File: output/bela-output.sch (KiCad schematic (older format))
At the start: 55 parts, among them P1 in_bela, P2 MTA-156-4, P3 out_mod, U1 TL074, U2 TL074, U3 TL072

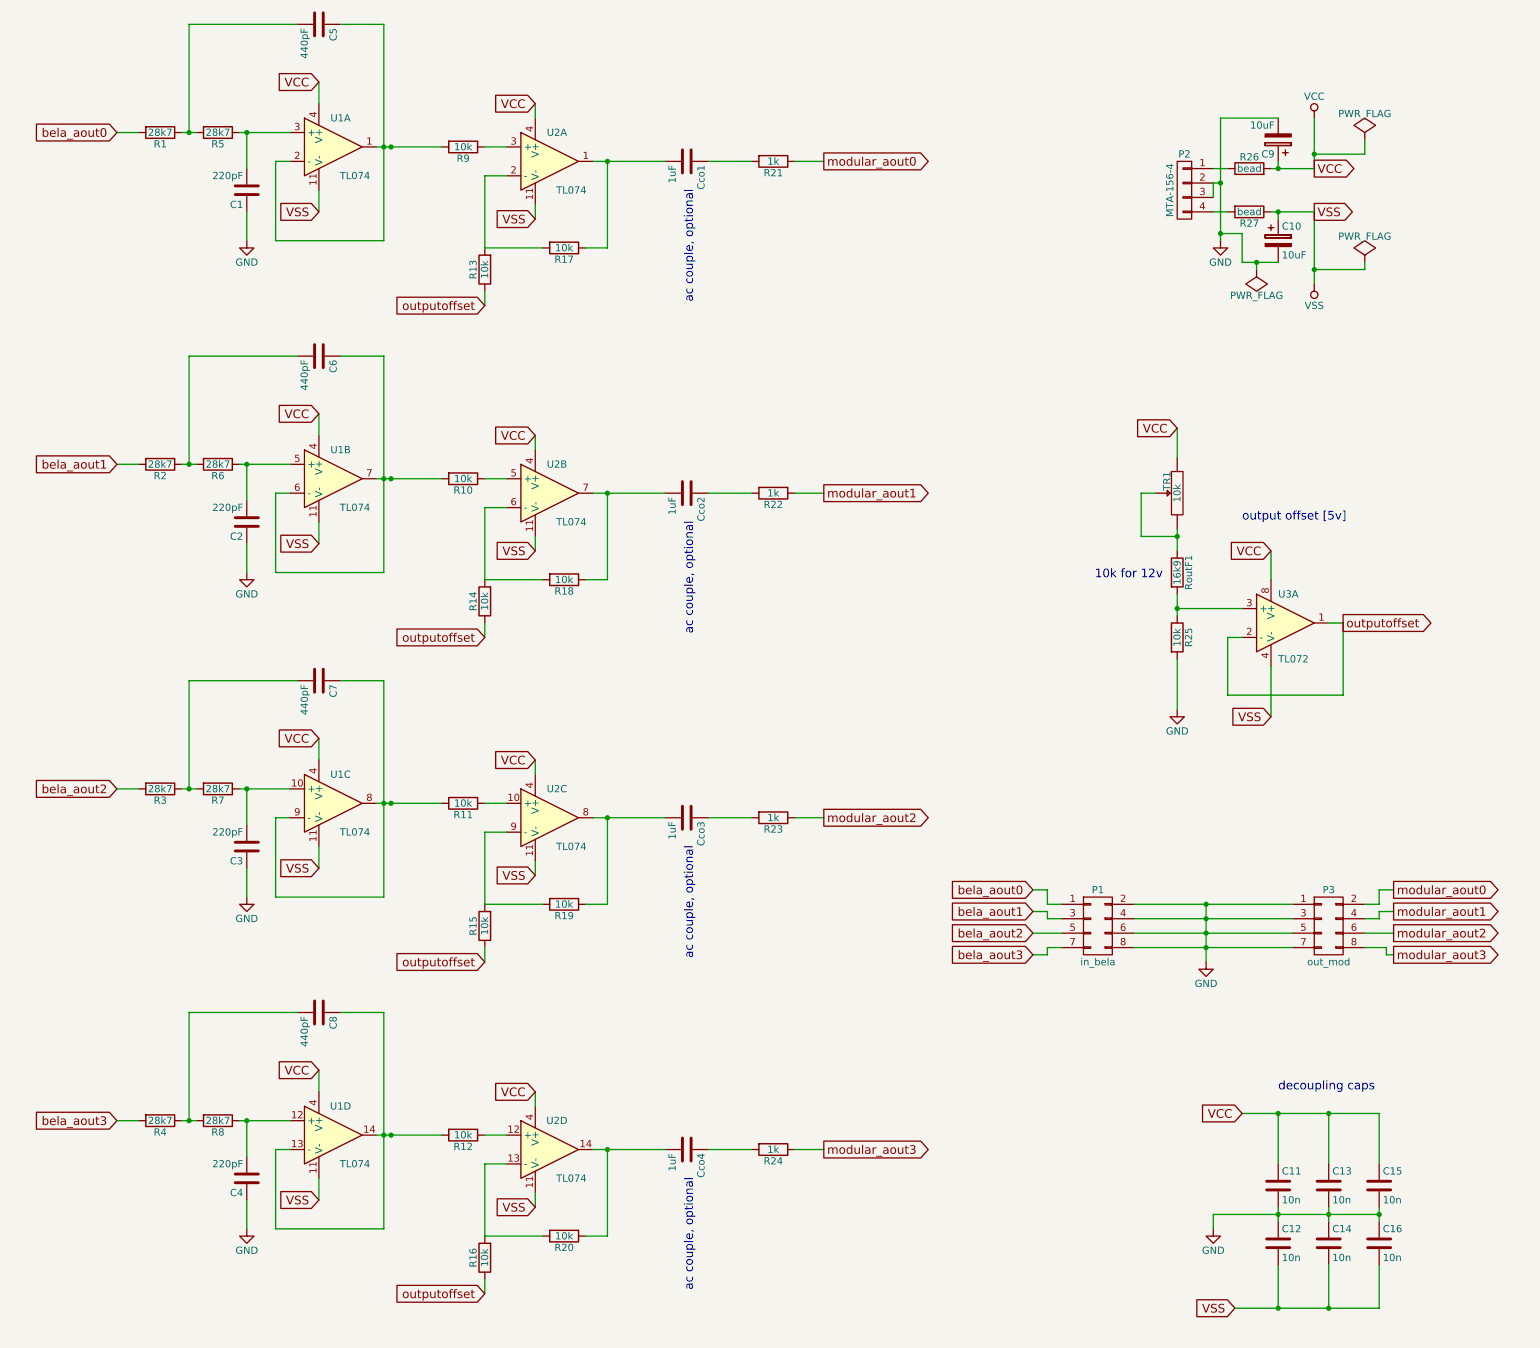
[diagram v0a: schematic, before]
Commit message: flush resistor layout
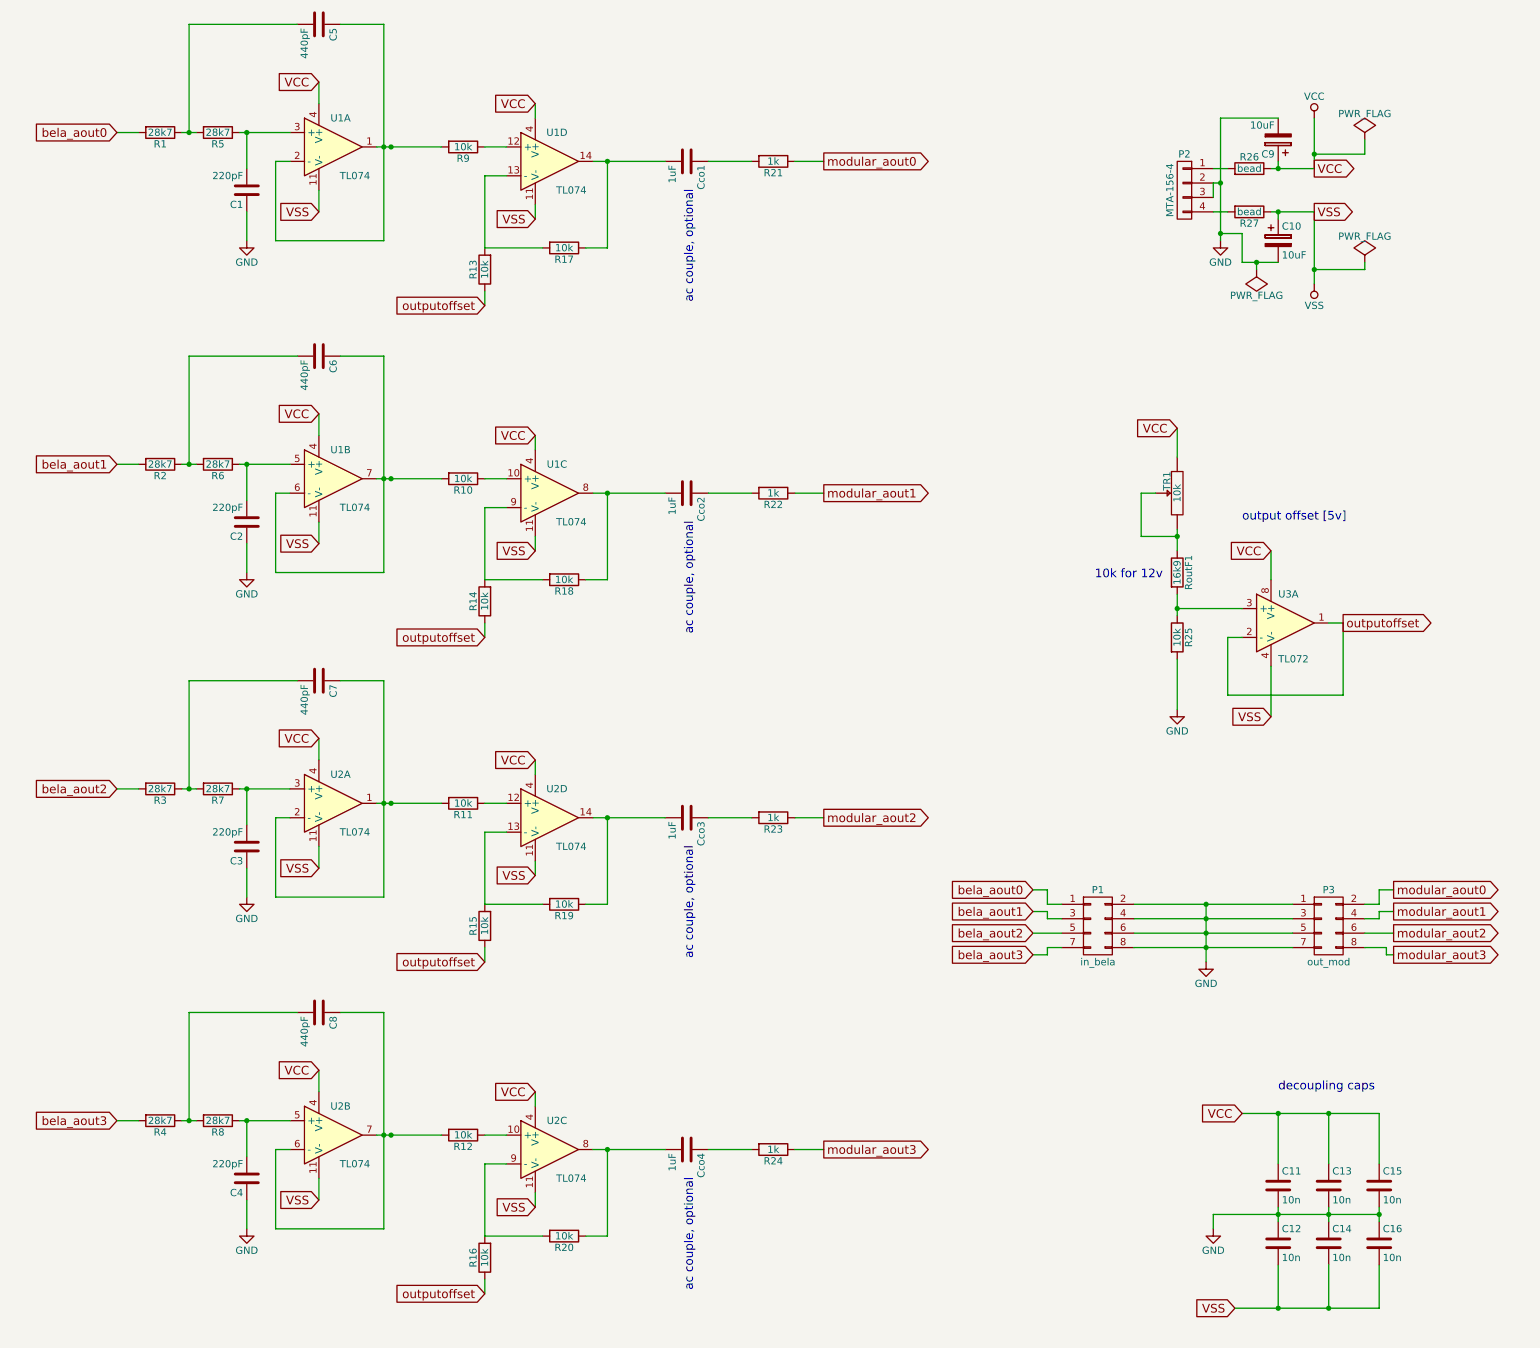
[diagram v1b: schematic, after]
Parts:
- R1, R10, R11, R12, R13, R14, R15, R16, R17, R18, R19, R2, R20, R21, R22, R23, R24, R25, R3, R4, R5, R6, R7, R8, R9, RoutF1: footprint Resistors_ThroughHole:Resistor_Vertical_RM5mm -> Resistors_ThroughHole:Resistor_Horizontal_RM10mm
- renumbered U2 to U1, U1 to U2
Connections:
- net VCC: now also R26.1; no longer R26.2
- net at Cco1.2, R17.1: now also U1.14; no longer U1.1
- net at R9.1: now also U1.12 (+); no longer U1.3 (+)
- net at R13.2, R17.2: now also U1.13 (-); no longer U1.2 (-)
- net at Cco2.2, R18.1: now also U1.8; no longer U1.7
- net at R10.1: now also U1.10 (+); no longer U1.5 (+)
- net at R14.2, R18.2: now also U1.9 (-); no longer U1.6 (-)
- net at Cco3.2, R19.1: now also U2.14; no longer U2.8
- net at R11.1: now also U2.12 (+); no longer U2.10 (+)
- net at C7.1, R11.2: now also U2.1, U2.2 (-); no longer U2.8, U2.9 (-)
- net at R15.2, R19.2: now also U2.13 (-); no longer U2.9 (-)
- net at C3.2, R7.1: now also U2.3 (+); no longer U2.10 (+)
- net at Cco4.2, R20.1: now also U2.8; no longer U2.14
- net at R12.1: now also U2.10 (+); no longer U2.12 (+)
- net at C8.1, R12.2: now also U2.6 (-), U2.7; no longer U2.13 (-), U2.14
- net at R16.2, R20.2: now also U2.9 (-); no longer U2.13 (-)
- net at C4.2, R8.1: now also U2.5 (+); no longer U2.12 (+)
- net at P2.1 (P1): now also R26.2; no longer R26.1
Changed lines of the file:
@@
 LIBS:trim
 LIBS:bela-output-cache
-LIBS:bela-input-cache
 EELAYER 25 0
 EELAYER END
@@
 F 0 "R9" V 3580 1600 50  0000 C CNN
 F 1 "10k" V 3500 1600 50  0000 C CNN
-F 2 "Resistors_ThroughHole:Resistor_Vertical_RM5mm" V 3430 1600 50  0001 C CNN
+F 2 "Resistors_ThroughHole:Resistor_Horizontal_RM10mm" V 3430 1600 50  0001 C CNN
 F 3 "" H 3500 1600 50  0000 C CNN
 	1    3500 1600
@@
 F 0 "R13" V 3730 2450 50  0000 C CNN
 F 1 "10k" V 3650 2450 50  0000 C CNN
-F 2 "Resistors_ThroughHole:Resistor_Vertical_RM5mm" V 3580 2450 50  0001 C CNN
+F 2 "Resistors_ThroughHole:Resistor_Horizontal_RM10mm" V 3580 2450 50  0001 C CNN
 F 3 "" H 3650 2450 50  0000 C CNN
 	1    3650 2450
@@
 $EndComp
 $Comp
-L TL074 U2
-U 1 1 5846D2B4
+L TL074 U1
+U 4 1 5846D2B4
 P 4100 1700
-F 0 "U2" H 4150 1900 50  0000 C CNN
+F 0 "U1" H 4150 1900 50  0000 C CNN
 F 1 "TL074" H 4250 1500 50  0000 C CNN
 F 2 "Housings_DIP:DIP-14_W7.62mm_LongPads" H 4050 1800 50  0001 C CNN
 F 3 "" H 4150 1900 50  0000 C CNN
-	1    4100 1700
+	4    4100 1700
 	1    0    0    -1
 $EndComp
@@
 F 0 "R17" V 4280 2300 50  0000 C CNN
 F 1 "10k" V 4200 2300 50  0000 C CNN
-F 2 "Resistors_ThroughHole:Resistor_Vertical_RM5mm" V 4130 2300 50  0001 C CNN
+F 2 "Resistors_ThroughHole:Resistor_Horizontal_RM10mm" V 4130 2300 50  0001 C CNN
 F 3 "" H 4200 2300 50  0000 C CNN
 	1    4200 2300
@@
 F 0 "R1" V 1480 1500 50  0000 C CNN
 F 1 "28k7" V 1400 1500 50  0000 C CNN
-F 2 "Resistors_ThroughHole:Resistor_Vertical_RM5mm" V 1330 1500 50  0001 C CNN
+F 2 "Resistors_ThroughHole:Resistor_Horizontal_RM10mm" V 1330 1500 50  0001 C CNN
 F 3 "" H 1400 1500 50  0000 C CNN
 	1    1400 1500
@@
 F 0 "R5" V 1880 1500 50  0000 C CNN
 F 1 "28k7" V 1800 1500 50  0000 C CNN
-F 2 "Resistors_ThroughHole:Resistor_Vertical_RM5mm" V 1730 1500 50  0001 C CNN
+F 2 "Resistors_ThroughHole:Resistor_Horizontal_RM10mm" V 1730 1500 50  0001 C CNN
 F 3 "" H 1800 1500 50  0000 C CNN
 	1    1800 1500
@@
 F 0 "R21" V 5730 1700 50  0000 C CNN
 F 1 "1k" V 5650 1700 50  0000 C CNN
-F 2 "Resistors_ThroughHole:Resistor_Vertical_RM5mm" V 5580 1700 50  0001 C CNN
+F 2 "Resistors_ThroughHole:Resistor_Horizontal_RM10mm" V 5580 1700 50  0001 C CNN
 F 3 "" H 5650 1700 50  0000 C CNN
 	1    5650 1700
@@
 F 0 "R10" V 3580 3900 50  0000 C CNN
 F 1 "10k" V 3500 3900 50  0000 C CNN
-F 2 "Resistors_ThroughHole:Resistor_Vertical_RM5mm" V 3430 3900 50  0001 C CNN
+F 2 "Resistors_ThroughHole:Resistor_Horizontal_RM10mm" V 3430 3900 50  0001 C CNN
 F 3 "" H 3500 3900 50  0000 C CNN
 	1    3500 3900
@@
 F 0 "R14" V 3730 4750 50  0000 C CNN
 F 1 "10k" V 3650 4750 50  0000 C CNN
-F 2 "Resistors_ThroughHole:Resistor_Vertical_RM5mm" V 3580 4750 50  0001 C CNN
+F 2 "Resistors_ThroughHole:Resistor_Horizontal_RM10mm" V 3580 4750 50  0001 C CNN
 F 3 "" H 3650 4750 50  0000 C CNN
 	1    3650 4750
@@
 $EndComp
 $Comp
-L TL074 U2
-U 2 1 5846D2C0
+L TL074 U1
+U 3 1 5846D2C0
 P 4100 4000
-F 0 "U2" H 4150 4200 50  0000 C CNN
+F 0 "U1" H 4150 4200 50  0000 C CNN
 F 1 "TL074" H 4250 3800 50  0000 C CNN
 F 2 "Housings_DIP:DIP-14_W7.62mm_LongPads" H 4050 4100 50  0001 C CNN
 F 3 "" H 4150 4200 50  0000 C CNN
-	2    4100 4000
+	3    4100 4000
 	1    0    0    -1
 $EndComp
@@
 F 0 "R18" V 4280 4600 50  0000 C CNN
 F 1 "10k" V 4200 4600 50  0000 C CNN
-F 2 "Resistors_ThroughHole:Resistor_Vertical_RM5mm" V 4130 4600 50  0001 C CNN
+F 2 "Resistors_ThroughHole:Resistor_Horizontal_RM10mm" V 4130 4600 50  0001 C CNN
 F 3 "" H 4200 4600 50  0000 C CNN
 	1    4200 4600
@@
 F 0 "R2" V 1480 3800 50  0000 C CNN
 F 1 "28k7" V 1400 3800 50  0000 C CNN
-F 2 "Resistors_ThroughHole:Resistor_Vertical_RM5mm" V 1330 3800 50  0001 C CNN
+F 2 "Resistors_ThroughHole:Resistor_Horizontal_RM10mm" V 1330 3800 50  0001 C CNN
 F 3 "" H 1400 3800 50  0000 C CNN
 	1    1400 3800
@@
 F 0 "R6" V 1880 3800 50  0000 C CNN
 F 1 "28k7" V 1800 3800 50  0000 C CNN
-F 2 "Resistors_ThroughHole:Resistor_Vertical_RM5mm" V 1730 3800 50  0001 C CNN
+F 2 "Resistors_ThroughHole:Resistor_Horizontal_RM10mm" V 1730 3800 50  0001 C CNN
 F 3 "" H 1800 3800 50  0000 C CNN
 	1    1800 3800
@@
 F 0 "R22" V 5730 4000 50  0000 C CNN
 F 1 "1k" V 5650 4000 50  0000 C CNN
-F 2 "Resistors_ThroughHole:Resistor_Vertical_RM5mm" V 5580 4000 50  0001 C CNN
+F 2 "Resistors_ThroughHole:Resistor_Horizontal_RM10mm" V 5580 4000 50  0001 C CNN
 F 3 "" H 5650 4000 50  0000 C CNN
 	1    5650 4000
@@
 F 0 "R11" V 3580 6150 50  0000 C CNN
 F 1 "10k" V 3500 6150 50  0000 C CNN
-F 2 "Resistors_ThroughHole:Resistor_Vertical_RM5mm" V 3430 6150 50  0001 C CNN
+F 2 "Resistors_ThroughHole:Resistor_Horizontal_RM10mm" V 3430 6150 50  0001 C CNN
 F 3 "" H 3500 6150 50  0000 C CNN
 	1    3500 6150
@@
 F 0 "R15" V 3730 7000 50  0000 C CNN
 F 1 "10k" V 3650 7000 50  0000 C CNN
-F 2 "Resistors_ThroughHole:Resistor_Vertical_RM5mm" V 3580 7000 50  0001 C CNN
+F 2 "Resistors_ThroughHole:Resistor_Horizontal_RM10mm" V 3580 7000 50  0001 C CNN
 F 3 "" H 3650 7000 50  0000 C CNN
 	1    3650 7000
@@
 $Comp
 L TL074 U2
-U 3 1 5846D2CC
+U 4 1 5846D2CC
 P 4100 6250
 F 0 "U2" H 4150 6450 50  0000 C CNN
@@
 F 2 "Housings_DIP:DIP-14_W7.62mm_LongPads" H 4050 6350 50  0001 C CNN
 F 3 "" H 4150 6450 50  0000 C CNN
-	3    4100 6250
-	1    0    0    -1
-$EndComp
-$Comp
-L TL074 U1
-U 3 1 5846D2CD
+	4    4100 6250
+	1    0    0    -1
+$EndComp
+$Comp
+L TL074 U2
+U 1 1 5846D2CD
 P 2600 6150
-F 0 "U1" H 2650 6350 50  0000 C CNN
+F 0 "U2" H 2650 6350 50  0000 C CNN
 F 1 "TL074" H 2750 5950 50  0000 C CNN
 F 2 "Housings_DIP:DIP-14_W7.62mm_LongPads" H 2550 6250 50  0001 C CNN
 F 3 "" H 2650 6350 50  0000 C CNN
-	3    2600 6150
+	1    2600 6150
 	1    0    0    -1
 $EndComp
@@
 F 0 "R19" V 4280 6850 50  0000 C CNN
 F 1 "10k" V 4200 6850 50  0000 C CNN
-F 2 "Resistors_ThroughHole:Resistor_Vertical_RM5mm" V 4130 6850 50  0001 C CNN
+F 2 "Resistors_ThroughHole:Resistor_Horizontal_RM10mm" V 4130 6850 50  0001 C CNN
 F 3 "" H 4200 6850 50  0000 C CNN
 	1    4200 6850
@@
 F 0 "R3" V 1480 6050 50  0000 C CNN
 F 1 "28k7" V 1400 6050 50  0000 C CNN
-F 2 "Resistors_ThroughHole:Resistor_Vertical_RM5mm" V 1330 6050 50  0001 C CNN
+F 2 "Resistors_ThroughHole:Resistor_Horizontal_RM10mm" V 1330 6050 50  0001 C CNN
 F 3 "" H 1400 6050 50  0000 C CNN
 	1    1400 6050
@@
 F 0 "R7" V 1880 6050 50  0000 C CNN
 F 1 "28k7" V 1800 6050 50  0000 C CNN
-F 2 "Resistors_ThroughHole:Resistor_Vertical_RM5mm" V 1730 6050 50  0001 C CNN
+F 2 "Resistors_ThroughHole:Resistor_Horizontal_RM10mm" V 1730 6050 50  0001 C CNN
 F 3 "" H 1800 6050 50  0000 C CNN
 	1    1800 6050
@@
 F 0 "R23" V 5730 6250 50  0000 C CNN
 F 1 "1k" V 5650 6250 50  0000 C CNN
-F 2 "Resistors_ThroughHole:Resistor_Vertical_RM5mm" V 5580 6250 50  0001 C CNN
+F 2 "Resistors_ThroughHole:Resistor_Horizontal_RM10mm" V 5580 6250 50  0001 C CNN
 F 3 "" H 5650 6250 50  0000 C CNN
 	1    5650 6250
@@
 F 0 "R12" V 3580 8450 50  0000 C CNN
 F 1 "10k" V 3500 8450 50  0000 C CNN
-F 2 "Resistors_ThroughHole:Resistor_Vertical_RM5mm" V 3430 8450 50  0001 C CNN
+F 2 "Resistors_ThroughHole:Resistor_Horizontal_RM10mm" V 3430 8450 50  0001 C CNN
 F 3 "" H 3500 8450 50  0000 C CNN
 	1    3500 8450
@@
 F 0 "R16" V 3730 9300 50  0000 C CNN
 F 1 "10k" V 3650 9300 50  0000 C CNN
-F 2 "Resistors_ThroughHole:Resistor_Vertical_RM5mm" V 3580 9300 50  0001 C CNN
+F 2 "Resistors_ThroughHole:Resistor_Horizontal_RM10mm" V 3580 9300 50  0001 C CNN
 F 3 "" H 3650 9300 50  0000 C CNN
 	1    3650 9300
@@
 $Comp
 L TL074 U2
-U 4 1 5846D2D8
+U 3 1 5846D2D8
 P 4100 8550
 F 0 "U2" H 4150 8750 50  0000 C CNN
@@
 F 2 "Housings_DIP:DIP-14_W7.62mm_LongPads" H 4050 8650 50  0001 C CNN
 F 3 "" H 4150 8750 50  0000 C CNN
-	4    4100 8550
-	1    0    0    -1
-$EndComp
-$Comp
-L TL074 U1
-U 4 1 5846D2D9
+	3    4100 8550
+	1    0    0    -1
+$EndComp
+$Comp
+L TL074 U2
+U 2 1 5846D2D9
 P 2600 8450
-F 0 "U1" H 2650 8650 50  0000 C CNN
+F 0 "U2" H 2650 8650 50  0000 C CNN
 F 1 "TL074" H 2750 8250 50  0000 C CNN
 F 2 "Housings_DIP:DIP-14_W7.62mm_LongPads" H 2550 8550 50  0001 C CNN
 F 3 "" H 2650 8650 50  0000 C CNN
-	4    2600 8450
+	2    2600 8450
 	1    0    0    -1
 $EndComp
@@
 F 0 "R20" V 4280 9150 50  0000 C CNN
 F 1 "10k" V 4200 9150 50  0000 C CNN
-F 2 "Resistors_ThroughHole:Resistor_Vertical_RM5mm" V 4130 9150 50  0001 C CNN
+F 2 "Resistors_ThroughHole:Resistor_Horizontal_RM10mm" V 4130 9150 50  0001 C CNN
 F 3 "" H 4200 9150 50  0000 C CNN
 	1    4200 9150
@@
 F 0 "R4" V 1480 8350 50  0000 C CNN
 F 1 "28k7" V 1400 8350 50  0000 C CNN
-F 2 "Resistors_ThroughHole:Resistor_Vertical_RM5mm" V 1330 8350 50  0001 C CNN
+F 2 "Resistors_ThroughHole:Resistor_Horizontal_RM10mm" V 1330 8350 50  0001 C CNN
 F 3 "" H 1400 8350 50  0000 C CNN
 	1    1400 8350
@@
 F 0 "R8" V 1880 8350 50  0000 C CNN
 F 1 "28k7" V 1800 8350 50  0000 C CNN
-F 2 "Resistors_ThroughHole:Resistor_Vertical_RM5mm" V 1730 8350 50  0001 C CNN
+F 2 "Resistors_ThroughHole:Resistor_Horizontal_RM10mm" V 1730 8350 50  0001 C CNN
 F 3 "" H 1800 8350 50  0000 C CNN
 	1    1800 8350
@@
 F 0 "R24" V 5730 8550 50  0000 C CNN
 F 1 "1k" V 5650 8550 50  0000 C CNN
-F 2 "Resistors_ThroughHole:Resistor_Vertical_RM5mm" V 5580 8550 50  0001 C CNN
+F 2 "Resistors_ThroughHole:Resistor_Horizontal_RM10mm" V 5580 8550 50  0001 C CNN
 F 3 "" H 5650 8550 50  0000 C CNN
 	1    5650 8550
@@
 F 0 "R25" V 8530 5000 50  0000 C CNN
 F 1 "10k" V 8450 5000 50  0000 C CNN
-F 2 "Resistors_ThroughHole:Resistor_Vertical_RM5mm" V 8380 5000 50  0001 C CNN
+F 2 "Resistors_ThroughHole:Resistor_Horizontal_RM10mm" V 8380 5000 50  0001 C CNN
 F 3 "" H 8450 5000 50  0000 C CNN
 	1    8450 5000
@@
 F 0 "RoutF1" V 8530 4550 50  0000 C CNN
 F 1 "16k9" V 8450 4550 50  0000 C CNN
-F 2 "Resistors_ThroughHole:Resistor_Vertical_RM5mm" V 8380 4550 50  0001 C CNN
+F 2 "Resistors_ThroughHole:Resistor_Horizontal_RM10mm" V 8380 4550 50  0001 C CNN
 F 3 "" H 8450 4550 50  0000 C CNN
 	1    8450 4550
@@
 F 3 "" H 8950 1750 50  0000 C CNN
 	1    8950 1750
-	0    -1   -1   0
-$EndComp
-$Comp
+	0    1    -1   0
+$EndComp
+$Comp
